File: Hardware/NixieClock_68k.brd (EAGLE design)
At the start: 96.8 x 100 mm, 50 parts, among them IC1 68008, IC10 7805, IC11 MIC803, IC12 74HC08N, IC2 AS6C1008, IC3 39SF020, IC4 DS1244Y, IC5 68681, IC6 74HC30N, IC7 74HC04N, IC8 74HC138N, IC9 74HC266N, Q1 3.6864MHz

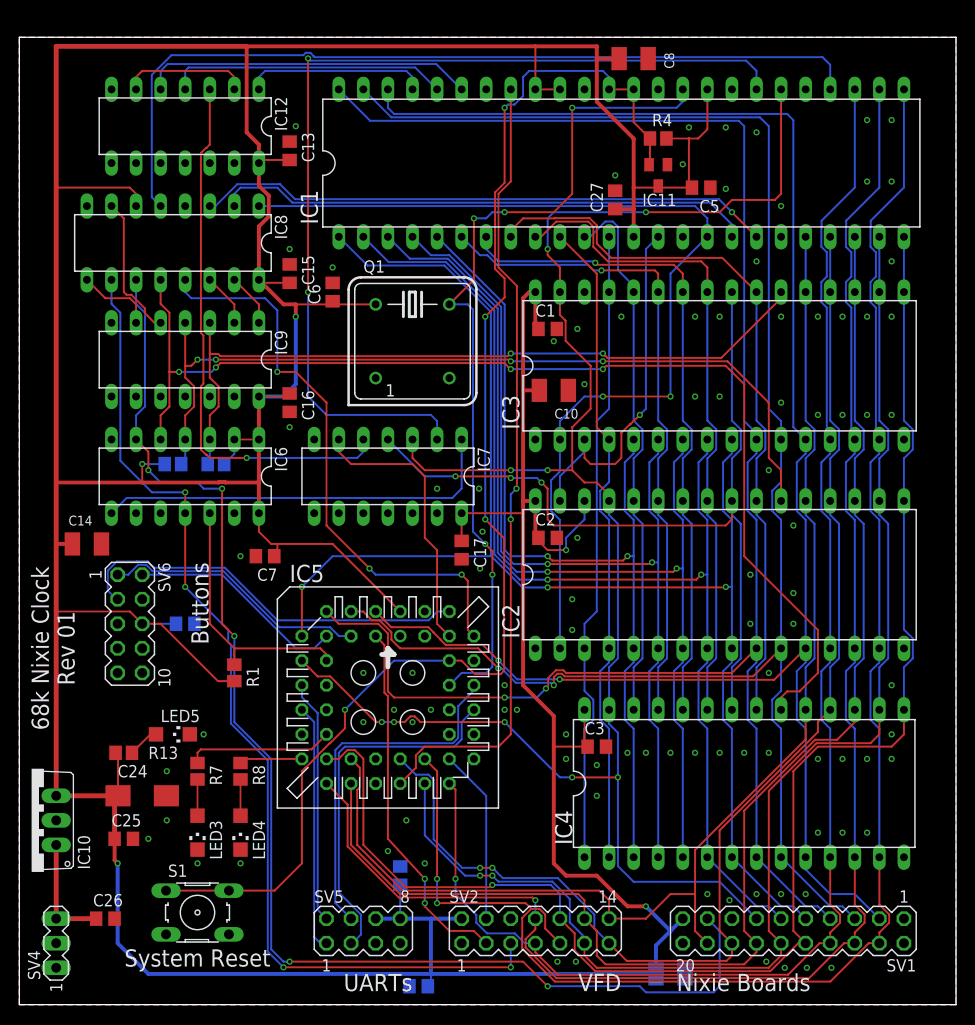
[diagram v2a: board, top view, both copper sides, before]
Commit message: added data bus resistors; better reset circuit
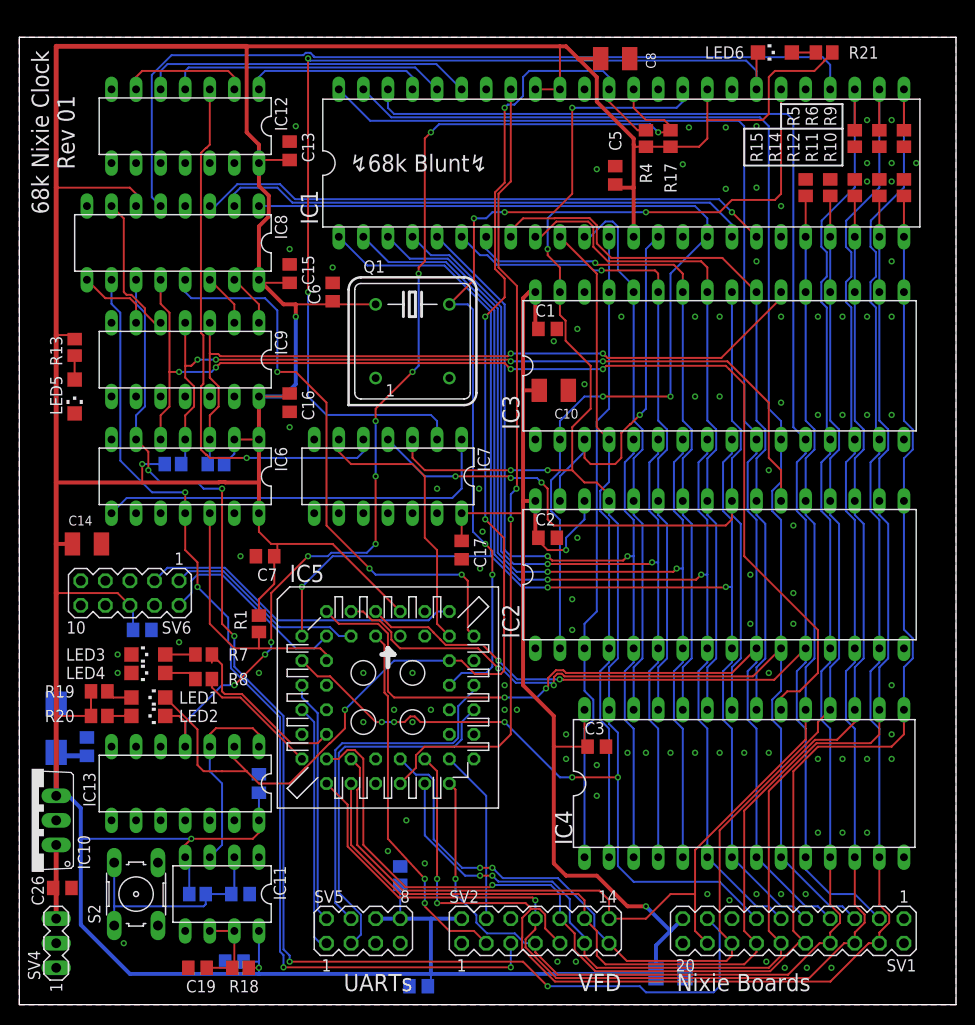
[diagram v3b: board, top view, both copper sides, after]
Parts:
- removed C27: 100nF, rcl:C0805
- removed S1: (no value), switch-omron:B3F-10XX
- added C12, C18, C19, C20: 100nF, rcl:C0805
- added IC13: 74HC05, 74xx-eu:DIL14
- added LED1, LED2, LED6: (no value), led:CHIPLED_1206
- added R10, R11, R12, R14, R15, R17, R5, R6, R9: 10k, rcl:R2012
- added R16, R18: 1M, rcl:R2012
- added R19, R20, R21: 3k, rcl:R2012
- added S2: (no value), switch-omron:B3F-10XX
- IC11: value MIC803 -> NE555; device Parts:SOT23C -> st-microelectronics:DIL-08
- moved IC11 86.9 mm to (21.0, 11.4)
- moved R13 42.2 mm to (5.71, 67.9), turned to 270 degrees
- moved LED5 36.4 mm to (5.71, 62.9), turned to 180 degrees
- moved LED3 19.1 mm to (13.3, 36.2), turned to 90 degrees
- moved LED4 19.1 mm to (13.3, 34.3), turned to 90 degrees
- moved R7 12.1 mm to (19.1, 36.2), turned to 180 degrees
- moved C24 11.3 mm to (3.81, 28.6), flipped to the bottom, turned to 90 degrees
- moved C25 10.3 mm to (6.99, 26.7), flipped to the bottom, turned to 90 degrees
- moved R8 10.3 mm to (19.1, 33.7), turned to 180 degrees
- moved C5 8.98 mm to (61.6, 85.7), turned to 90 degrees
- moved R1 5.68 mm to (24.8, 39.4), turned to 90 degrees
- moved C26 5.46 mm to (4.45, 12.1)
- moved C28 4.49 mm to (12.7, 38.7)
- moved SV6 3.18 mm to (11.4, 42.5), turned to 180 degrees
- moved C8 1.91 mm to (61.6, 97.8)
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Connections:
- new net !HALT: IC1.36, IC13.4, LED2.C, R17.1
- new net N$1: C18.1, IC11.2, R16.2, S2.1, S2.2
- new net N$10: LED6.A, R21.2
- new net N$12: C19.1, IC11.6, IC11.7, R18.2
- new net N$2: LED1.A, R19.2
- new net N$6: LED2.A, R20.2
- new net RESET: IC11.3, IC13.1, IC13.3
- net !DTACK: now also LED6.C
- net !RESET: now also IC13.2, LED1.C; no longer IC1.36, IC11.2, S1.1, S1.2
- net +5V: now also C12.1, C20.1, IC11.4, IC11.8, IC13.14, R16.1, R17.2, R18.1, R19.1, R20.1, R21.1; no longer C27.1, IC11.3
- net D0: now also R5.2
- net D1: now also R6.2
- net D2: now also R9.2
- net D3: now also R10.2
- net D4: now also R11.2
- net D5: now also R12.2
- net D6: now also R14.2
- net D7: now also R15.2
- net GND: now also C12.2, C18.2, C19.2, C20.2, IC11.5, IC12.10, IC12.12, IC12.13, IC12.9, IC13.11, IC13.13, IC13.5, IC13.7, IC13.9, IC7.11, IC7.13, IC7.9, IC9.12, IC9.13, IC9.8, IC9.9, R10.1, R11.1, R12.1, R14.1, R15.1, R5.1, R6.1, R9.1, S2.3, S2.4; no longer C27.2, S1.3, S1.4
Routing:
- net !HALT: track 0.00 -> 115.4 mm, vias 0 -> 11
- net +5V: track 571.0 -> 618.4 mm, vias 5 -> 6
- net N$1: track 0.00 -> 23.7 mm
- net RESET: track 0.00 -> 20.6 mm
- net N$12: track 0.00 -> 9.08 mm
- net SW2: track 42.1 -> 33.7 mm
- net SW0: track 27.6 -> 21.0 mm
- net STATUS0: track 6.77 -> 13.2 mm
- net !RESET: track 139.0 -> 133.1 mm
- net D7: track 129.4 -> 133.7 mm
- net D6: track 128.7 -> 132.9 mm
- net D4: track 135.3 -> 139.5 mm
- net D5: track 138.6 -> 142.8 mm
- net D3: track 152.8 -> 157.0 mm
- net D2: track 168.1 -> 172.3 mm
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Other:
- board text added: "↯68k Blunt↯"
- board text removed: "Buttons"
- board text removed: "System Reset"

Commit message: basic 68681 initialization; more nixie driver routines and ram defines
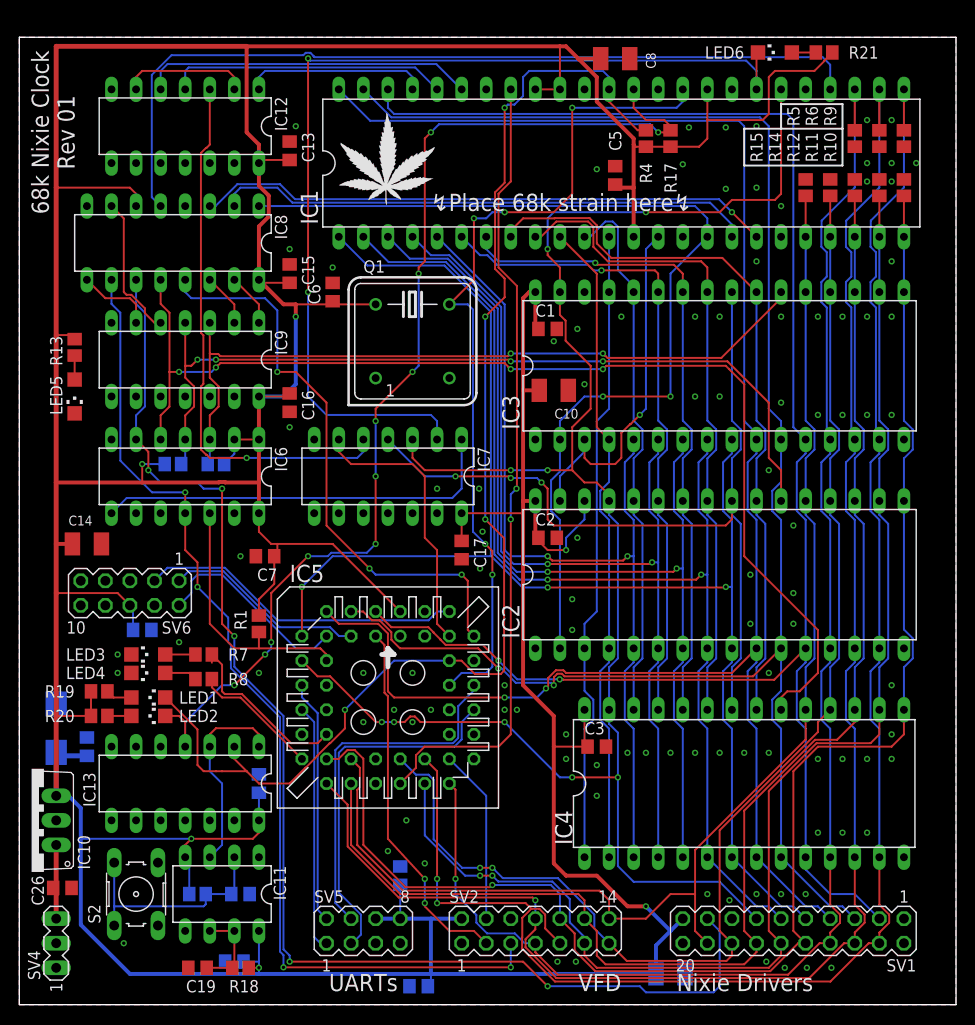
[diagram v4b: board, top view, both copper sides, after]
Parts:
- added WEED1: WEED, Parts:DOINK
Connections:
- removed net !IPL0/2: IC1.42
- net GND: now also IC1.42
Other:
- board text added: "Nixie Drivers"
- board text added: "↯Place 68k strain here↯"
- board text removed: "Nixie Boards"
- board text removed: "↯68k Blunt↯"
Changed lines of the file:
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@@
 <wire x1="0" y1="100" x2="0" y2="0" width="0" layer="20"/>
 <text x="62.23" y="3.175" size="1.778" layer="25" rot="R180">VFD</text>
-<text x="67.945" y="3.175" size="1.778" layer="25" rot="R180" align="bottom-right">Nixie Boards</text>
+<text x="67.945" y="3.175" size="1.778" layer="25" rot="R180" align="bottom-right">Nixie Drivers</text>
 <text x="1.27" y="90.17" size="1.778" layer="25" rot="R90" align="top-center">68k Nixie Clock
 Rev 01</text>
-<text x="40.64" y="3.175" size="1.778" layer="25" rot="R180">UARTs</text>
+<text x="35.56" y="3.175" size="1.778" layer="25" rot="R180" align="bottom-center">UARTs</text>
 <wire x1="74.93" y1="86.741" x2="85.09" y2="86.741" width="0.2032" layer="25"/>
 <wire x1="85.09" y1="86.741" x2="85.09" y2="90.551" width="0.2032" layer="25"/>
@@
 <wire x1="85.09" y1="93.091" x2="78.74" y2="93.091" width="0.2032" layer="25"/>
 <wire x1="78.74" y1="93.091" x2="78.74" y2="90.551" width="0.2032" layer="25"/>
-<text x="41.275" y="86.995" size="1.778" layer="25" align="center">↯68k Blunt↯</text>
+<text x="42.545" y="83.82" size="1.778" layer="25" align="top-left">↯Place 68k strain here↯</text>
 </plain>
 <attributes>
@@
 <attribute name="VALUE" x="79.375" y="100.965" size="1.27" layer="27" rot="R180"/>
 </element>
+<element name="WEED1" library="Parts" package="DOINK" value="WEED" x="33.02" y="82.55" smashed="yes"/>
 </elements>
 <signals>
@@
 <contactref element="IC9" pad="9"/>
 <contactref element="IC9" pad="12"/>
+<contactref element="IC1" pad="42"/>
 </signal>
 <signal name="CLK">
@@
 <wire x1="51.435" y1="53.388" x2="51.435" y2="74.295" width="0.2032" layer="1"/>
 </signal>
-<signal name="!IPL0/2">
-<contactref element="IC1" pad="42"/>
-</signal>
 <signal name="!BG">

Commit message: updated rom/ram chip select logic
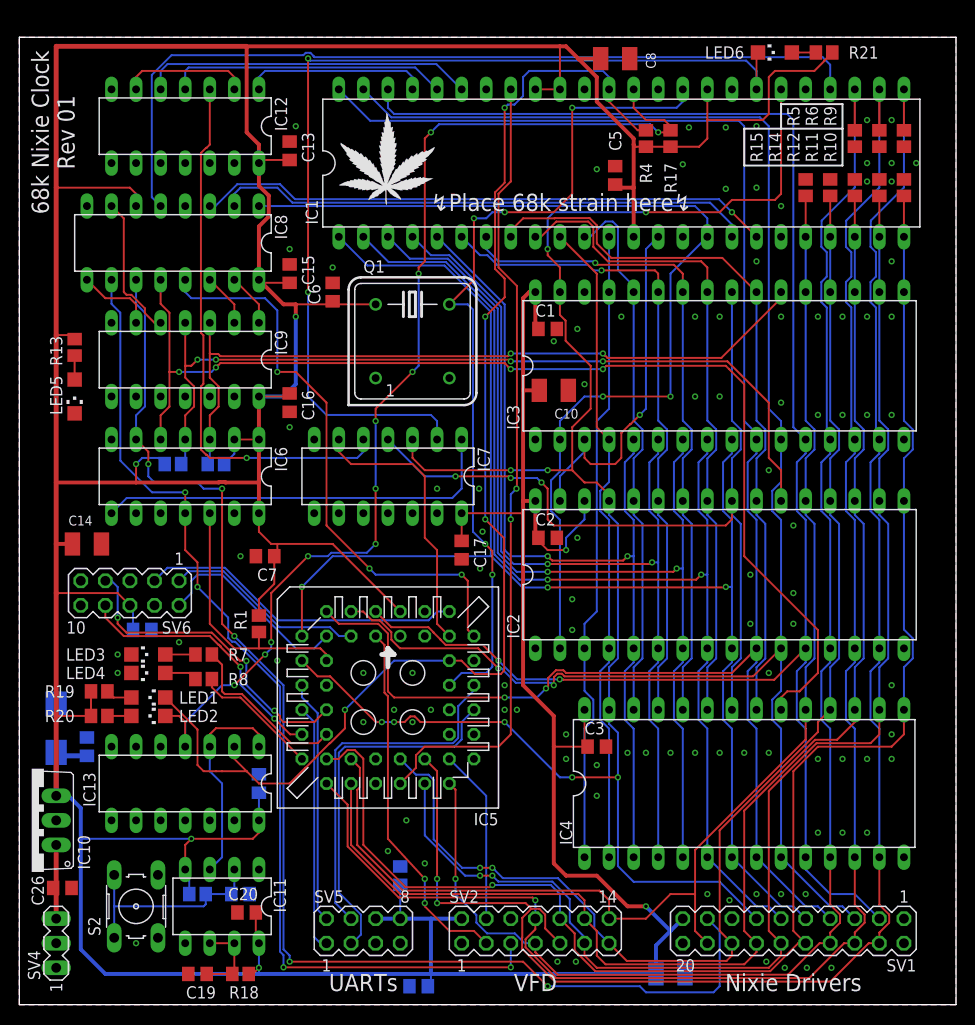
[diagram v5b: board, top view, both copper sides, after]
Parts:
- IC9: value 74HC266N -> 74HC7266
- moved C20 5.24 mm to (23.5, 9.53), flipped to the top, turned to 180 degrees
- moved IC11 1.27 mm to (21.0, 10.2)
- moved S2 1.27 mm to (12.1, 10.2)
- moved C19 0.64 mm to (18.4, 3.17)
- moved R18 0.64 mm to (22.9, 3.17)
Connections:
- net OUT0: now also IC5.15
- net OUT1: now also IC5.14
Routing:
- net OUT1: track 0.00 -> 33.3 mm, vias 0 -> 3
- net OUT0: track 0.00 -> 27.7 mm, vias 0 -> 2
- net +5V: track 618.4 -> 621.8 mm
- net RESET: track 20.6 -> 21.9 mm
- net N$1: track 23.7 -> 22.4 mm
- net STATUS1: track 18.5 -> 17.6 mm
- net N$12: track 9.08 -> 8.45 mm

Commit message: revamped power connections; moved power regulation to separate board (plus RS232 conversion)
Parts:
- removed C26: 100nF, rcl:C0805
- removed IC10: 7805, linear:TO220V
- removed SV4: (no value), con-lstb:MA03-1
- added C21: 100nF, rcl:C0805
- added SV3: (no value), con-lstb:MA03-2
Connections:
- removed net N$8: C26.1, IC10.1, SV4.3
- net +5V: now also C21.1, SV3.1, SV3.3, SV3.5; no longer IC10.3
- net GND: now also C21.2, SV3.2, SV3.4, SV3.6; no longer C26.2, IC10.2, SV4.1
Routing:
- net N$8: track 8.39 -> 0.00 mm
- net +5V: track 621.8 -> 618.7 mm, vias 6 -> 7

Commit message: more uart stuff in loader
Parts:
- IC3: value 39SF020 -> 39SF010
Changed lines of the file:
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@@
 <?xml version="1.0" encoding="utf-8"?>
 <!DOCTYPE eagle SYSTEM "eagle.dtd">
-<eagle version="9.3.0">
+<eagle version="9.3.2">
 <drawing>
 <settings>
@@
 <attribute name="VALUE" x="94.234" y="37.719" size="1.27" layer="27" rot="R90" align="top-left"/>
 </element>
-<element name="IC3" library="Parts" package="DIL32" package3d_urn="urn:adsk.eagle:package:18076/2" value="39SF020" x="72.39" y="66.04" smashed="yes">
-<attribute name="MOUSER" value="804-39SF020A7CPHE" x="151.13" y="10.16" size="1.778" layer="27" display="off"/>
+<element name="IC3" library="Parts" package="DIL32" package3d_urn="urn:adsk.eagle:package:18076/2" value="39SF010" x="72.39" y="66.04" smashed="yes">
+<attribute name="MOUSER" value="804-39SF010A7CPHE" x="151.13" y="10.16" size="1.778" layer="27" display="off"/>
 <attribute name="NAME" x="51.689" y="59.436" size="1.27" layer="25" rot="R90"/>
 <attribute name="VALUE" x="94.234" y="59.944" size="1.27" layer="27" rot="R90" align="top-left"/>

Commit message: basic app and updated checksum handling
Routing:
- net CLK: track 88.7 -> 87.8 mm
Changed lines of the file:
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@@
 <?xml version="1.0" encoding="utf-8"?>
 <!DOCTYPE eagle SYSTEM "eagle.dtd">
-<eagle version="9.3.2">
+<eagle version="9.2.1">
 <drawing>
 <settings>
@@
 <via x="43.18" y="53.34" extent="1-16" drill="0.35"/>
 <via x="47.879" y="48.895" extent="1-16" drill="0.35"/>
-<via x="47.625" y="45.085" extent="1-16" drill="0.35"/>
+<via x="46.99" y="44.45" extent="1-16" drill="0.35"/>
 <via x="50.165" y="33.02" extent="1-16" drill="0.35"/>
 <via x="41.91" y="14.605" extent="1-16" drill="0.35"/>
@@
 <contactref element="C24" pad="-"/>
 <contactref element="C21" pad="2"/>
+<via x="48.895" y="37.465" extent="1-16" drill="0.35"/>
 </signal>
 <signal name="CLK">
@@
 <contactref element="IC5" pad="36"/>
 <wire x1="44.45" y1="33.02" x2="45.72" y2="34.29" width="0.2032" layer="16"/>
-<wire x1="45.72" y1="34.29" x2="48.26" y2="34.29" width="0.2032" layer="16"/>
-<wire x1="48.26" y1="34.29" x2="48.895" y2="34.925" width="0.2032" layer="16"/>
-<wire x1="48.895" y1="34.925" x2="48.895" y2="44.45" width="0.2032" layer="16"/>
-<via x="48.895" y="44.45" extent="1-16" drill="0.35"/>
-<wire x1="48.895" y1="44.45" x2="48.895" y2="46.8912" width="0.2032" layer="1"/>
-<wire x1="48.895" y1="46.8912" x2="48.1612" y2="47.625" width="0.2032" layer="1"/>
+<wire x1="45.72" y1="34.29" x2="47.625" y2="34.29" width="0.2032" layer="16"/>
+<wire x1="47.625" y1="34.29" x2="48.26" y2="34.925" width="0.2032" layer="16"/>
+<wire x1="48.26" y1="44.45" x2="48.26" y2="34.925" width="0.2032" layer="16"/>
+<via x="48.26" y="44.45" extent="1-16" drill="0.35"/>
+<wire x1="48.26" y1="44.45" x2="48.26" y2="47.5262" width="0.2032" layer="1"/>
+<wire x1="48.26" y1="47.5262" x2="48.1612" y2="47.625" width="0.2032" layer="1"/>
 <via x="48.1612" y="47.625" extent="1-16" drill="0.35"/>
 <wire x1="46.8912" y1="71.8538" x2="46.8912" y2="48.895" width="0.2032" layer="16"/>
